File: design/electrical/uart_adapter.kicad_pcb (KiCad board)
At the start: 2 copper layers, 33.2 x 42.7 mm, 15 parts, among them J1 DB9, P1 CONN_01X04, P2 CONN_01X04, U1 MAX3227

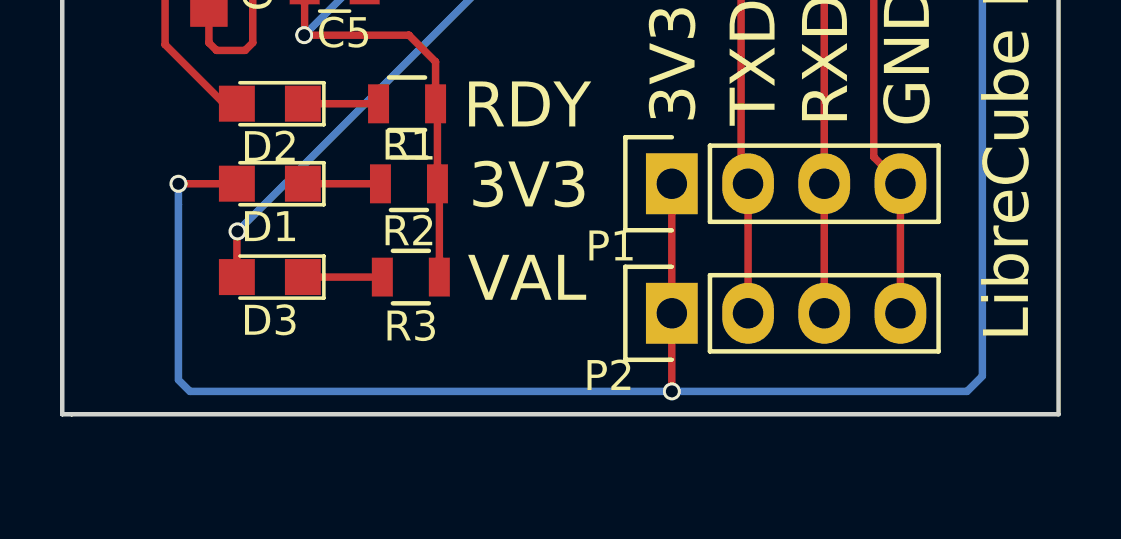
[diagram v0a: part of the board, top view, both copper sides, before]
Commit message: Added Molex connector
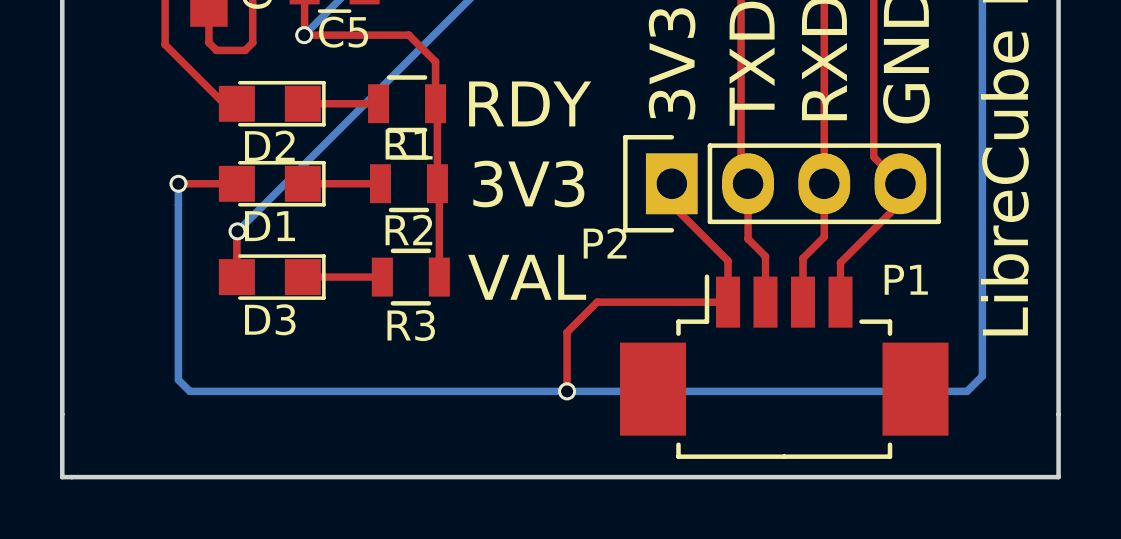
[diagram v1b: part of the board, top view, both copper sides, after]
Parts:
- P1: footprint Socket_Strips:Socket_Strip_Straight_1x04 -> Connectors_Molex:Molex_PicoBlade_53261-0471_04x1.25mm_Angled
- moved P1 3.90 mm to (156.7, 103.8)
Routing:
- net +3V3: track 78.3 -> 83.9 mm
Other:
- board size 33.2 x 42.7 mm -> 33.2 x 44.8 mm
